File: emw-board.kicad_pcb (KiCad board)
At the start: 2 copper layers, 49.5 x 48.3 mm, 34 parts, among them P1 1WIRE, P2 BATT, P3 CONN_01X06, P4 SWD, P5 CONS, P6 OLED, P7 CONN_01X07, SW1 B3S-1000, SW2 B3S-1000, U1 MAX604CSA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

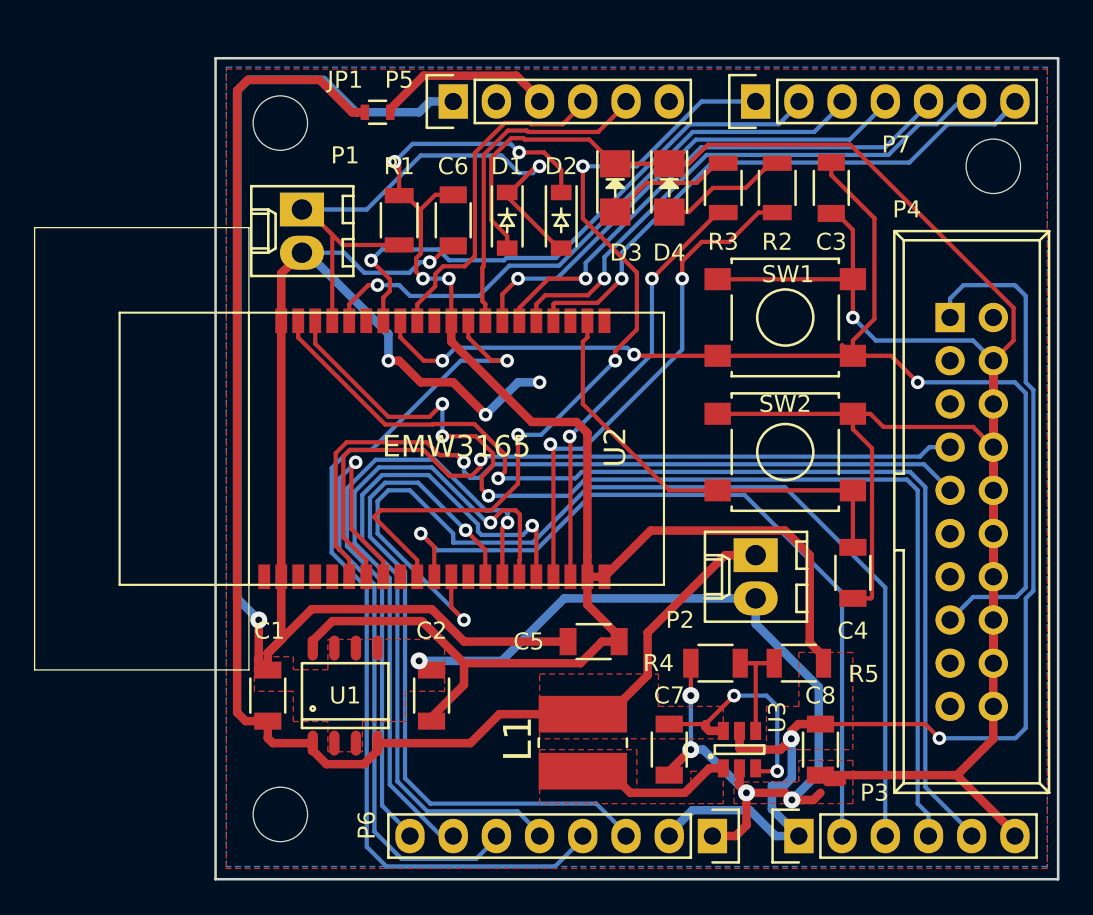
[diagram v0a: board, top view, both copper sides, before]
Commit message: Reposition buttons. New SWD connector. Reposition power connector.
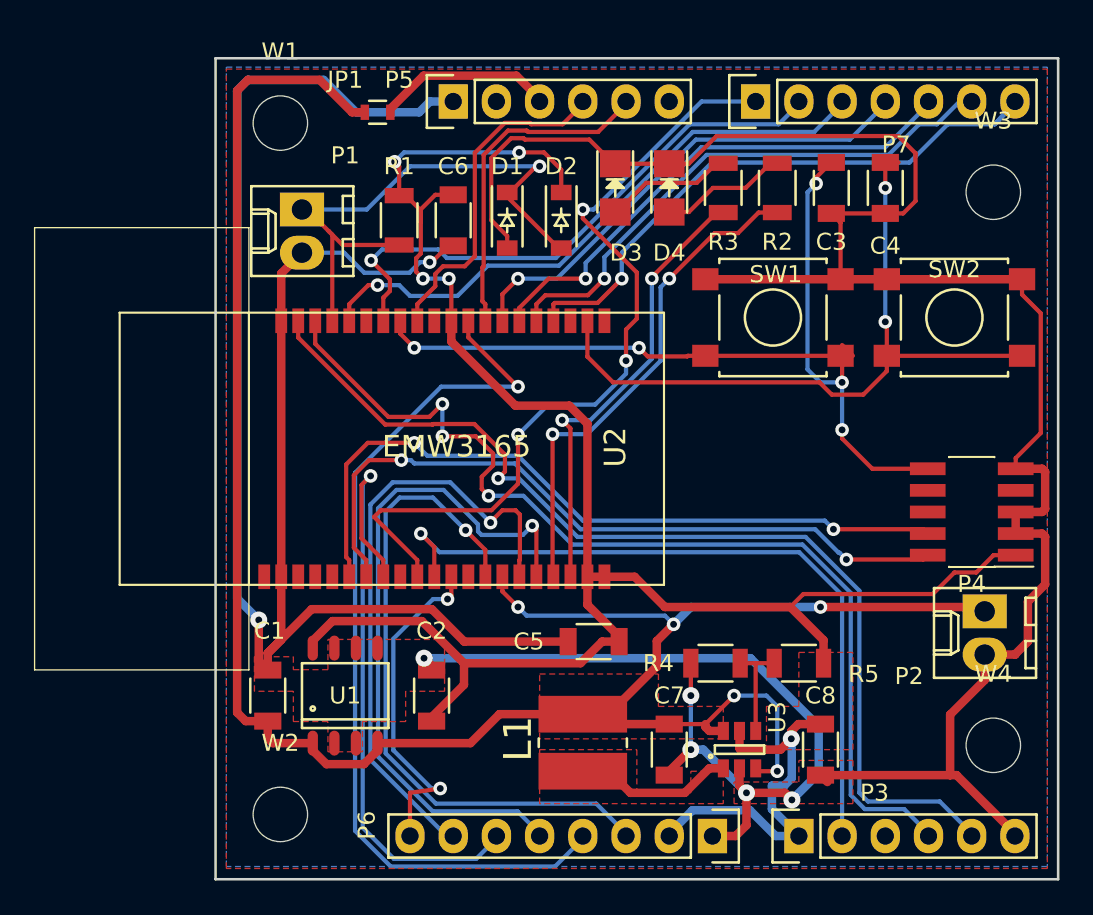
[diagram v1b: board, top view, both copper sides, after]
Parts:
- removed REF** (x3): MountingHole_3.2mm_M3, Mounting_Holes:MountingHole_3.2mm_M3
- added W1: TEST_1P, Mounting_Holes:MountingHole_3.2mm_M3, F.Cu at (118.1, 57.1)
- added W2: TEST_1P, Mounting_Holes:MountingHole_3.2mm_M3, F.Cu at (118.1, 97.8)
- added W3: TEST_1P, Mounting_Holes:MountingHole_3.2mm_M3, F.Cu at (160.0, 61.2)
- added W4: TEST_1P, Mounting_Holes:MountingHole_3.2mm_M3, F.Cu at (160.0, 93.7)
- P4: value SWD -> SWDN; footprint Connect:IDC_Header_Straight_20pins -> Pin_Headers:Pin_Header_Straight_2x05_Pitch1.27mm_SMD
- moved C4 22.7 mm to (153.7, 61.0)
- moved P2 13.9 mm to (159.5, 85.9)
- moved SW2 12.7 mm to (157.7, 68.6)
- moved P4 11.5 mm to (158.8, 80.0), turned to 180 degrees
- moved SW1 0.72 mm to (147.1, 68.6)
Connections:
- P3 pad 3: PB8 -> Net-(P3-Pad3)
- P4 pad 10: GND -> Net-(C3-Pad1)
- P4 pad 3: Net-(P4-Pad3) -> GND
- P4 pad 4: GND -> Net-(P4-Pad4)
- P4 pad 5: Net-(P4-Pad5) -> GND
- P4 pad 6: GND -> Net-(P4-Pad6)
- P4 pad 8: GND -> Net-(P4-Pad8)
- P4 pad 9: Net-(P4-Pad9) -> GND
- U2 pad 25: Net-(P4-Pad9) -> Net-(P4-Pad4)
- U2 pad 26: Net-(P4-Pad7) -> Net-(P4-Pad2)
- U2 pad 31: PB8 -> OLED_CS
- U2 pad 34: OLED_CS -> +BATT
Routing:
- net GND: track 338.2 -> 270.9 mm, vias 11 -> 7
- net PB8: track 62.7 -> 0.00 mm, vias 1 -> 0
- net Net-(P4-Pad9): track 46.1 -> 0.00 mm, vias 1 -> 0
- net Net-(P4-Pad7): track 45.0 -> 0.00 mm, vias 1 -> 0
- net Net-(P4-Pad4): track 0.00 -> 43.6 mm, vias 0 -> 2
- net Net-(P4-Pad2): track 0.00 -> 42.9 mm, vias 0 -> 2
- net +3V3: track 165.8 -> 131.0 mm, vias 6 -> 5
- net +BATT: track 98.6 -> 127.6 mm, vias 2 -> 5
- net OLED_CS: track 37.3 -> 20.9 mm, vias 1 -> 2
- net SETUP: track 26.3 -> 42.3 mm, vias 0 -> 2
- net Net-(C3-Pad1): track 70.2 -> 54.6 mm, vias 3 -> 5
- net PB9: track 65.6 -> 60.3 mm
- net PB12: track 64.9 -> 61.2 mm
- net PB6: track 46.1 -> 43.3 mm
- net OLED_RST: track 43.0 -> 40.3 mm
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
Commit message: Add OSH logo.
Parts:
- added REF***: OSHW-Logo2_14.6x12mm_SilkScreen, Symbols:OSHW-Logo2_14.6x12mm_SilkScreen, B.Cu at (148.1, 76.5)
